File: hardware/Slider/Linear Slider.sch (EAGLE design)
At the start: 9 parts

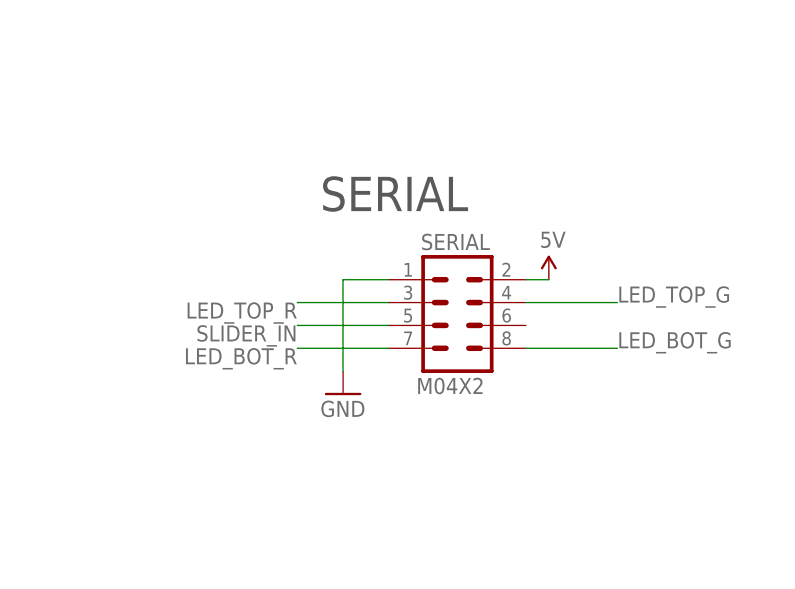
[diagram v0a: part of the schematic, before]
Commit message: Ordered Version
Small mechanical changes
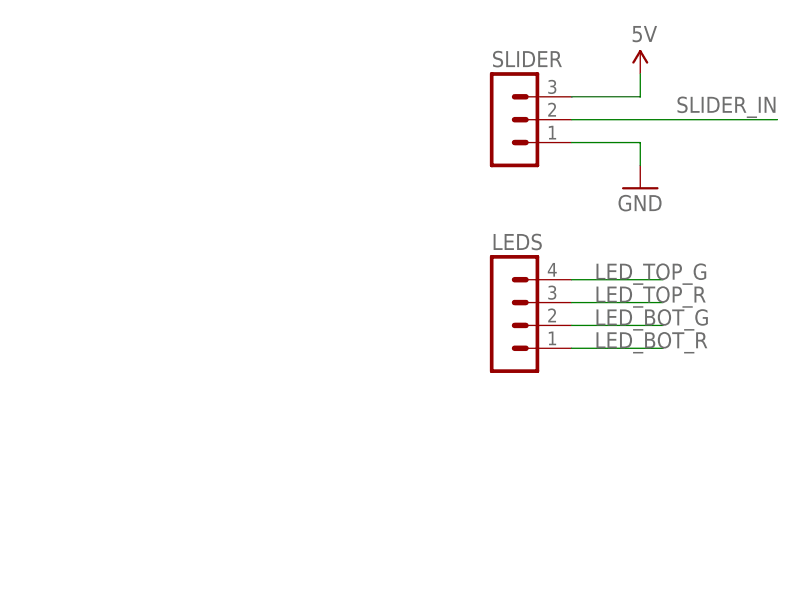
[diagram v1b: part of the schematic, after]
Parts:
- removed SERIAL: M04X2, SparkFun:M04X2
- added LEDS: (no value), con-lstb:MA04-1
- added SLIDER: (no value), con-lstb:MA03-1
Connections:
- net 5V: no longer SERIAL.2
- net GND: no longer SERIAL.1
- net LED_BOT_G: now also LEDS.2; no longer SERIAL.8
- net LED_BOT_R: now also LEDS.1; no longer SERIAL.7
- net LED_TOP_G: now also LEDS.4; no longer SERIAL.4
- net LED_TOP_R: now also LEDS.3; no longer SERIAL.3
- net SLIDER_IN: now also SLIDER.2; no longer SERIAL.5
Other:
- note removed: "SERIAL"
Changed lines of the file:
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@@
 <part name="POT1" library="SKAARHOJ" deviceset="SLIDER" device="60" value="10K Linear"/>
 <part name="C1" library="SparkFun" deviceset="CAP" device="0603-CAP" value="10nF"/>
-<part name="SERIAL" library="SparkFun" deviceset="M04X2" device=""/>
 <part name="GND5" library="SparkFun" deviceset="GND" device=""/>
 <part name="U$17" library="SparkFun" deviceset="5V" device=""/>
@@
 <part name="R4" library="resistor" deviceset="R-EU_" device="R0603" value="180"/>
 <part name="FRAME1" library="frames" deviceset="A4L-LOC" device="" value="Linear Slider"/>
+<part name="SLIDER" library="con-lstb" deviceset="MA03-1" device=""/>
+<part name="LEDS" library="con-lstb" deviceset="MA04-1" device=""/>
 </parts>
 <sheets>
 <sheet>
 <plain>
-<text x="172.72" y="124.46" size="3.81" layer="97">SERIAL</text>
 </plain>
 <instances>
 <instance part="POT1" gate="G$1" x="165.1" y="68.58"/>
 <instance part="C1" gate="G$1" x="190.5" y="63.5"/>
-<instance part="SERIAL" gate="G$1" x="187.96" y="111.76"/>
-<instance part="GND5" gate="1" x="175.26" y="104.14"/>
-<instance part="U$17" gate="G$1" x="198.12" y="116.84"/>
+<instance part="GND5" gate="1" x="208.28" y="127"/>
+<instance part="U$17" gate="G$1" x="208.28" y="139.7"/>
 <instance part="LD1" gate="G$1" x="50.8" y="109.22"/>
 <instance part="LD2" gate="G$1" x="50.8" y="68.58"/>
@@
 <instance part="R4" gate="G$1" x="60.96" y="58.42"/>
 <instance part="FRAME1" gate="G$1" x="0" y="0"/>
+<instance part="SLIDER" gate="G$1" x="193.04" y="134.62"/>
+<instance part="LEDS" gate="1" x="193.04" y="114.3"/>
 </instances>
 <busses>
@@
 <net name="5V" class="1">
 <segment>
-<pinref part="SERIAL" gate="G$1" pin="2"/>
 <pinref part="U$17" gate="G$1" pin="5V"/>
-<wire x1="195.58" y1="116.84" x2="198.12" y2="116.84" width="0.1524" layer="91"/>
+<wire x1="200.66" y1="137.16" x2="208.28" y2="137.16" width="0.1524" layer="91"/>
+<wire x1="208.28" y1="137.16" x2="208.28" y2="139.7" width="0.1524" layer="91"/>
 </segment>
 <segment>
@@
 <net name="GND" class="1">
 <segment>
-<pinref part="SERIAL" gate="G$1" pin="1"/>
-<wire x1="180.34" y1="116.84" x2="175.26" y2="116.84" width="0.1524" layer="91"/>
+<wire x1="200.66" y1="132.08" x2="208.28" y2="132.08" width="0.1524" layer="91"/>
 <pinref part="GND5" gate="1" pin="GND"/>
-<wire x1="175.26" y1="116.84" x2="175.26" y2="106.68" width="0.1524" layer="91"/>
+<wire x1="208.28" y1="132.08" x2="208.28" y2="129.54" width="0.1524" layer="91"/>
 </segment>
 <segment>
@@
 <net name="SLIDER_IN" class="0">
 <segment>
-<pinref part="SERIAL" gate="G$1" pin="5"/>
-<wire x1="180.34" y1="111.76" x2="170.18" y2="111.76" width="0.1524" layer="91"/>
-<label x="170.18" y="111.76" size="1.778" layer="95" rot="R180"/>
+<wire x1="200.66" y1="134.62" x2="223.52" y2="134.62" width="0.1524" layer="91"/>
+<label x="223.52" y="137.16" size="1.778" layer="95" rot="R180"/>
+<pinref part="SLIDER" gate="G$1" pin="2"/>
 </segment>
 <segment>
@@
 </segment>
 <segment>
-<pinref part="SERIAL" gate="G$1" pin="3"/>
-<wire x1="180.34" y1="114.3" x2="170.18" y2="114.3" width="0.1524" layer="91"/>
-<label x="170.18" y="114.3" size="1.778" layer="95" rot="R180"/>
+<wire x1="210.82" y1="114.3" x2="200.66" y2="114.3" width="0.1524" layer="91"/>
+<label x="203.2" y="114.3" size="1.778" layer="95"/>
+<pinref part="LEDS" gate="1" pin="3"/>
 </segment>
 </net>
@@
 </segment>
 <segment>
-<pinref part="SERIAL" gate="G$1" pin="4"/>
-<wire x1="195.58" y1="114.3" x2="205.74" y2="114.3" width="0.1524" layer="91"/>
-<label x="205.74" y="114.3" size="1.778" layer="95"/>
+<wire x1="200.66" y1="116.84" x2="210.82" y2="116.84" width="0.1524" layer="91"/>
+<label x="203.2" y="116.84" size="1.778" layer="95"/>
+<pinref part="LEDS" gate="1" pin="4"/>
 </segment>
 </net>
@@
 </segment>
 <segment>
-<pinref part="SERIAL" gate="G$1" pin="7"/>
-<wire x1="180.34" y1="109.22" x2="170.18" y2="109.22" width="0.1524" layer="91"/>
-<label x="170.18" y="109.22" size="1.778" layer="95" rot="R180"/>
+<wire x1="210.82" y1="109.22" x2="200.66" y2="109.22" width="0.1524" layer="91"/>
+<label x="203.2" y="109.22" size="1.778" layer="95"/>
+<pinref part="LEDS" gate="1" pin="1"/>
 </segment>
 </net>
@@
 </segment>
 <segment>
-<pinref part="SERIAL" gate="G$1" pin="8"/>
-<wire x1="195.58" y1="109.22" x2="205.74" y2="109.22" width="0.1524" layer="91"/>
-<label x="205.74" y="109.22" size="1.778" layer="95"/>
+<wire x1="200.66" y1="111.76" x2="210.82" y2="111.76" width="0.1524" layer="91"/>
+<label x="203.2" y="111.76" size="1.778" layer="95"/>
+<pinref part="LEDS" gate="1" pin="2"/>
 </segment>
 </net>

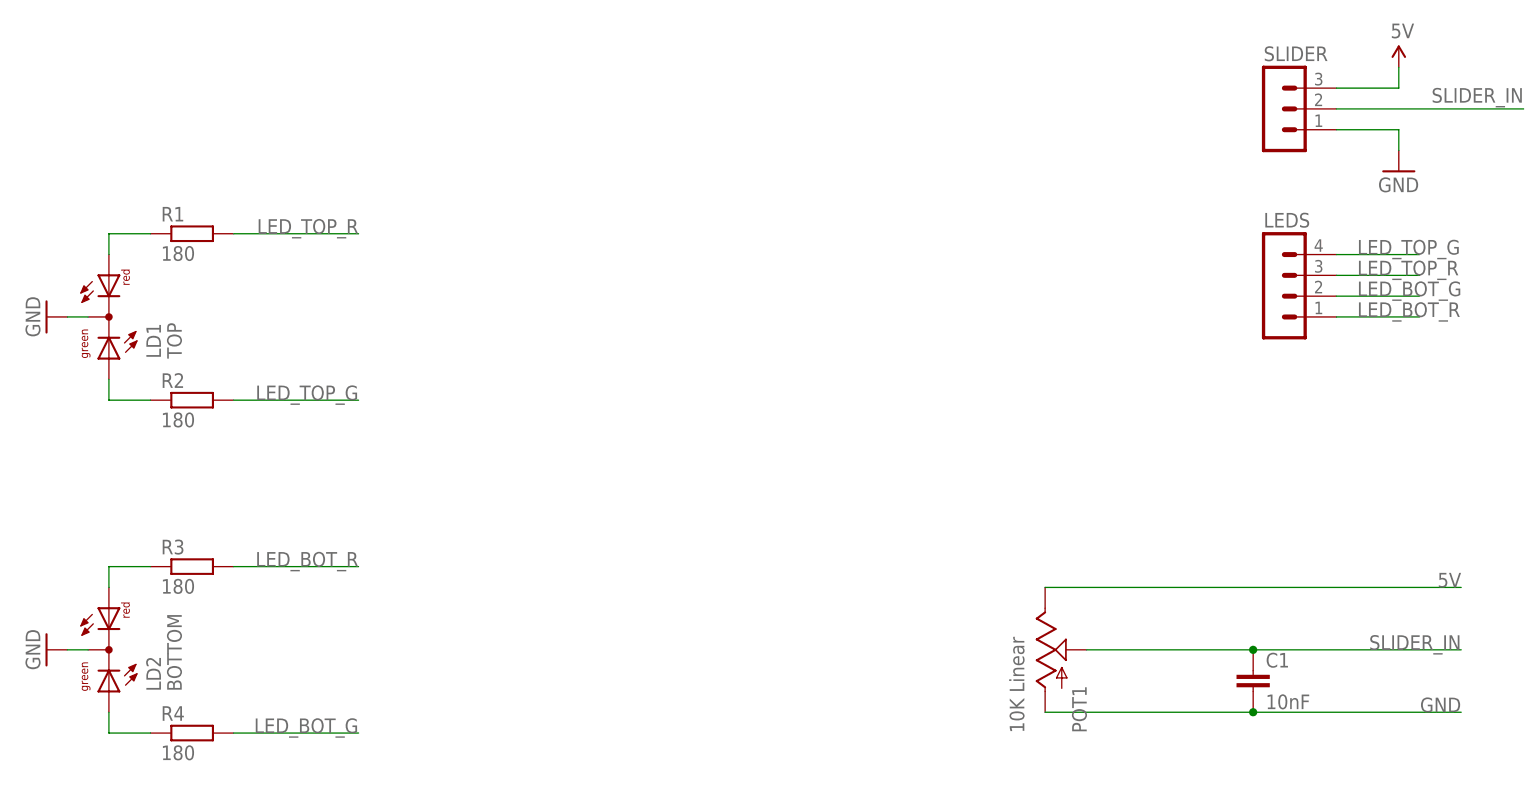
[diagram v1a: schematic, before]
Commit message: New version of slider board
Common anode, molex conn. (ordered)
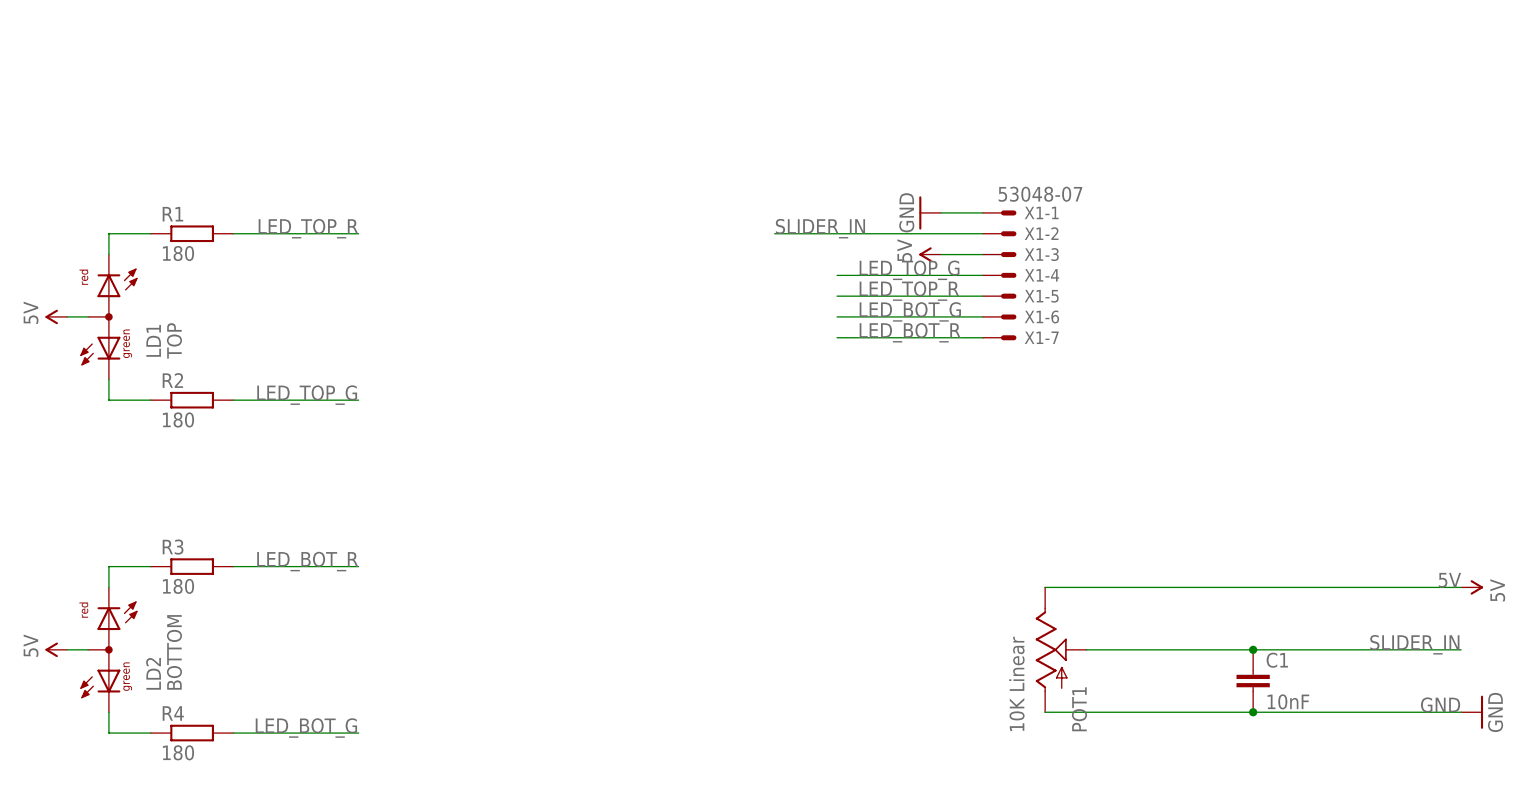
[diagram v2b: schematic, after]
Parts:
- removed LEDS: (no value), con-lstb:MA04-1
- removed SLIDER: (no value), con-lstb:MA03-1
- added X1: 53048-07, con-molex:53048-07
- LD1, LD2: device led:DUOLED-RG-C -> led:DUOLED-RG-A
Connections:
- net 5V: now also LD1.A, LD2.A, X1-3.S
- net GND: now also X1-1.S; no longer LD1.C, LD2.C
- net LED_BOT_G: now also X1-6.S; no longer LEDS.2
- net LED_BOT_R: now also X1-7.S; no longer LEDS.1
- net LED_TOP_G: now also X1-4.S; no longer LEDS.4
- net LED_TOP_R: now also X1-5.S; no longer LEDS.3
- net N$1: now also LD1.CR; no longer LD1.AR
- net N$2: now also LD1.CG; no longer LD1.AG
- net N$3: now also LD2.CG; no longer LD2.AG
- net N$4: now also LD2.CR; no longer LD2.AR
- net SLIDER_IN: now also X1-2.S; no longer SLIDER.2
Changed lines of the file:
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@@
 <part name="POT1" library="SKAARHOJ" deviceset="SLIDER" device="60" value="10K Linear"/>
 <part name="C1" library="SparkFun" deviceset="CAP" device="0603-CAP" value="10nF"/>
-<part name="GND5" library="SparkFun" deviceset="GND" device=""/>
-<part name="U$17" library="SparkFun" deviceset="5V" device=""/>
-<part name="LD1" library="led" deviceset="DUOLED-RG-C" device="" value="TOP"/>
-<part name="LD2" library="led" deviceset="DUOLED-RG-C" device="" value="BOTTOM"/>
-<part name="GND1" library="SparkFun" deviceset="GND" device=""/>
-<part name="GND2" library="SparkFun" deviceset="GND" device=""/>
+<part name="LD1" library="led" deviceset="DUOLED-RG-A" device="" value="TOP"/>
+<part name="LD2" library="led" deviceset="DUOLED-RG-A" device="" value="BOTTOM"/>
 <part name="R1" library="resistor" deviceset="R-EU_" device="R0603" value="180"/>
 <part name="R2" library="resistor" deviceset="R-EU_" device="R0603" value="180"/>
@@
 <part name="R4" library="resistor" deviceset="R-EU_" device="R0603" value="180"/>
 <part name="FRAME1" library="frames" deviceset="A4L-LOC" device="" value="Linear Slider"/>
-<part name="SLIDER" library="con-lstb" deviceset="MA03-1" device=""/>
-<part name="LEDS" library="con-lstb" deviceset="MA04-1" device=""/>
+<part name="U$1" library="SparkFun" deviceset="5V" device=""/>
+<part name="U$2" library="SparkFun" deviceset="5V" device=""/>
+<part name="U$3" library="SparkFun" deviceset="5V" device=""/>
+<part name="GND1" library="SparkFun" deviceset="GND" device=""/>
+<part name="X1" library="con-molex" deviceset="53?-07" device="048"/>
+<part name="U$4" library="SparkFun" deviceset="5V" device=""/>
+<part name="GND2" library="SparkFun" deviceset="GND" device=""/>
 </parts>
 <sheets>
@@
 <instance part="POT1" gate="G$1" x="165.1" y="68.58"/>
 <instance part="C1" gate="G$1" x="190.5" y="63.5"/>
-<instance part="GND5" gate="1" x="208.28" y="127"/>
-<instance part="U$17" gate="G$1" x="208.28" y="139.7"/>
 <instance part="LD1" gate="G$1" x="50.8" y="109.22"/>
 <instance part="LD2" gate="G$1" x="50.8" y="68.58"/>
-<instance part="GND1" gate="1" x="43.18" y="109.22" rot="R270"/>
-<instance part="GND2" gate="1" x="43.18" y="68.58" rot="R270"/>
 <instance part="R1" gate="G$1" x="60.96" y="119.38"/>
 <instance part="R2" gate="G$1" x="60.96" y="99.06"/>
@@
 <instance part="R4" gate="G$1" x="60.96" y="58.42"/>
 <instance part="FRAME1" gate="G$1" x="0" y="0"/>
-<instance part="SLIDER" gate="G$1" x="193.04" y="134.62"/>
-<instance part="LEDS" gate="1" x="193.04" y="114.3"/>
+<instance part="U$1" gate="G$1" x="45.72" y="109.22" rot="R90"/>
+<instance part="U$2" gate="G$1" x="45.72" y="68.58" rot="R90"/>
+<instance part="U$3" gate="G$1" x="215.9" y="76.2" rot="R270"/>
+<instance part="GND1" gate="1" x="218.44" y="60.96" rot="R90"/>
+<instance part="X1" gate="-1" x="160.02" y="121.92"/>
+<instance part="X1" gate="-2" x="160.02" y="119.38"/>
+<instance part="X1" gate="-3" x="160.02" y="116.84"/>
+<instance part="X1" gate="-4" x="160.02" y="114.3"/>
+<instance part="X1" gate="-5" x="160.02" y="111.76"/>
+<instance part="X1" gate="-6" x="160.02" y="109.22"/>
+<instance part="X1" gate="-7" x="160.02" y="106.68"/>
+<instance part="U$4" gate="G$1" x="152.4" y="116.84" rot="R90"/>
+<instance part="GND2" gate="1" x="149.86" y="121.92" rot="R270"/>
 </instances>
 <busses>
@@
 <net name="5V" class="1">
 <segment>
-<pinref part="U$17" gate="G$1" pin="5V"/>
-<wire x1="200.66" y1="137.16" x2="208.28" y2="137.16" width="0.1524" layer="91"/>
-<wire x1="208.28" y1="137.16" x2="208.28" y2="139.7" width="0.1524" layer="91"/>
-</segment>
-<segment>
 <pinref part="POT1" gate="G$1" pin="E"/>
 <wire x1="165.1" y1="76.2" x2="215.9" y2="76.2" width="0.1524" layer="91"/>
 <label x="215.9" y="76.2" size="1.778" layer="95" rot="MR0"/>
+<pinref part="U$3" gate="G$1" pin="5V"/>
+</segment>
+<segment>
+<pinref part="U$2" gate="G$1" pin="5V"/>
+<pinref part="LD2" gate="G$1" pin="A"/>
+<wire x1="45.72" y1="68.58" x2="48.26" y2="68.58" width="0.1524" layer="91"/>
+</segment>
+<segment>
+<pinref part="U$1" gate="G$1" pin="5V"/>
+<pinref part="LD1" gate="G$1" pin="A"/>
+<wire x1="45.72" y1="109.22" x2="48.26" y2="109.22" width="0.1524" layer="91"/>
+</segment>
+<segment>
+<pinref part="U$4" gate="G$1" pin="5V"/>
+<pinref part="X1" gate="-3" pin="S"/>
+<wire x1="152.4" y1="116.84" x2="157.48" y2="116.84" width="0.1524" layer="91"/>
 </segment>
 </net>
 <net name="GND" class="1">
-<segment>
-<wire x1="200.66" y1="132.08" x2="208.28" y2="132.08" width="0.1524" layer="91"/>
-<pinref part="GND5" gate="1" pin="GND"/>
-<wire x1="208.28" y1="132.08" x2="208.28" y2="129.54" width="0.1524" layer="91"/>
-</segment>
 <segment>
 <pinref part="POT1" gate="G$1" pin="A"/>
@@
 <junction x="190.5" y="60.96"/>
 <label x="215.9" y="60.96" size="1.778" layer="95" rot="MR0"/>
+<pinref part="GND1" gate="1" pin="GND"/>
 </segment>
 <segment>
-<pinref part="LD1" gate="G$1" pin="C"/>
-<pinref part="GND1" gate="1" pin="GND"/>
-<wire x1="45.72" y1="109.22" x2="48.26" y2="109.22" width="0.1524" layer="91"/>
-</segment>
-<segment>
-<pinref part="LD2" gate="G$1" pin="C"/>
+<pinref part="X1" gate="-1" pin="S"/>
 <pinref part="GND2" gate="1" pin="GND"/>
-<wire x1="45.72" y1="68.58" x2="48.26" y2="68.58" width="0.1524" layer="91"/>
+<wire x1="157.48" y1="121.92" x2="152.4" y2="121.92" width="0.1524" layer="91"/>
 </segment>
 </net>
 <net name="SLIDER_IN" class="0">
 <segment>
-<wire x1="200.66" y1="134.62" x2="223.52" y2="134.62" width="0.1524" layer="91"/>
-<label x="223.52" y="137.16" size="1.778" layer="95" rot="R180"/>
-<pinref part="SLIDER" gate="G$1" pin="2"/>
+<label x="132.08" y="119.38" size="1.778" layer="95"/>
+<wire x1="157.48" y1="119.38" x2="132.08" y2="119.38" width="0.1524" layer="91"/>
+<pinref part="X1" gate="-2" pin="S"/>
 </segment>
 <segment>
@@
 <net name="N$1" class="0">
 <segment>
-<pinref part="LD1" gate="G$1" pin="AR"/>
+<pinref part="LD1" gate="G$1" pin="CR"/>
 <pinref part="R1" gate="G$1" pin="1"/>
 <wire x1="50.8" y1="116.84" x2="50.8" y2="119.38" width="0.1524" layer="91"/>
@@
 <net name="N$2" class="0">
 <segment>
-<pinref part="LD1" gate="G$1" pin="AG"/>
+<pinref part="LD1" gate="G$1" pin="CG"/>
 <pinref part="R2" gate="G$1" pin="1"/>
 <wire x1="50.8" y1="101.6" x2="50.8" y2="99.06" width="0.1524" layer="91"/>
@@
 <net name="N$3" class="0">
 <segment>
-<pinref part="LD2" gate="G$1" pin="AG"/>
+<pinref part="LD2" gate="G$1" pin="CG"/>
 <pinref part="R4" gate="G$1" pin="1"/>
 <wire x1="50.8" y1="60.96" x2="50.8" y2="58.42" width="0.1524" layer="91"/>
@@
 <net name="N$4" class="0">
 <segment>
-<pinref part="LD2" gate="G$1" pin="AR"/>
+<pinref part="LD2" gate="G$1" pin="CR"/>
 <pinref part="R3" gate="G$1" pin="1"/>
 <wire x1="50.8" y1="76.2" x2="50.8" y2="78.74" width="0.1524" layer="91"/>
@@
 </segment>
 <segment>
-<wire x1="210.82" y1="114.3" x2="200.66" y2="114.3" width="0.1524" layer="91"/>
-<label x="203.2" y="114.3" size="1.778" layer="95"/>
-<pinref part="LEDS" gate="1" pin="3"/>
+<wire x1="157.48" y1="111.76" x2="139.7" y2="111.76" width="0.1524" layer="91"/>
+<label x="142.24" y="111.76" size="1.778" layer="95"/>
+<pinref part="X1" gate="-5" pin="S"/>
 </segment>
 </net>
@@
 </segment>
 <segment>
-<wire x1="200.66" y1="116.84" x2="210.82" y2="116.84" width="0.1524" layer="91"/>
-<label x="203.2" y="116.84" size="1.778" layer="95"/>
-<pinref part="LEDS" gate="1" pin="4"/>
+<wire x1="157.48" y1="114.3" x2="139.7" y2="114.3" width="0.1524" layer="91"/>
+<label x="142.24" y="114.3" size="1.778" layer="95"/>
+<pinref part="X1" gate="-4" pin="S"/>
 </segment>
 </net>
@@
 </segment>
 <segment>
-<wire x1="210.82" y1="109.22" x2="200.66" y2="109.22" width="0.1524" layer="91"/>
-<label x="203.2" y="109.22" size="1.778" layer="95"/>
-<pinref part="LEDS" gate="1" pin="1"/>
+<wire x1="157.48" y1="106.68" x2="139.7" y2="106.68" width="0.1524" layer="91"/>
+<label x="142.24" y="106.68" size="1.778" layer="95"/>
+<pinref part="X1" gate="-7" pin="S"/>
 </segment>
 </net>
@@
 </segment>
 <segment>
-<wire x1="200.66" y1="111.76" x2="210.82" y2="111.76" width="0.1524" layer="91"/>
-<label x="203.2" y="111.76" size="1.778" layer="95"/>
-<pinref part="LEDS" gate="1" pin="2"/>
+<wire x1="139.7" y1="109.22" x2="157.48" y2="109.22" width="0.1524" layer="91"/>
+<label x="142.24" y="109.22" size="1.778" layer="95"/>
+<pinref part="X1" gate="-6" pin="S"/>
 </segment>
 </net>
